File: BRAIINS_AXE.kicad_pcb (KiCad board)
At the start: 6 copper layers, 105.5 x 181.1 mm, 230 parts, among them J1 RJ45_Hanrun_HR911105A_Horizon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, J10 Connector 02x01, J2 Conn_01x06, J9 Conn_01x10, M1 Fan_4pin, M2 Fan_4pin, U10 BM1370_mode1, U11 BM1370_mode1, U15 W5500, U16 CSD95472Q5MC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

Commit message: alingment
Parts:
- moved C190 4.31 mm to (54.1, 63.5)
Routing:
- net +1V2: track 217.1 -> 216.9 mm, vias 9 -> 8
- net VDD: vias 137 -> 148
- net GND: vias 337 -> 297
- net +12V: vias 20 -> 1

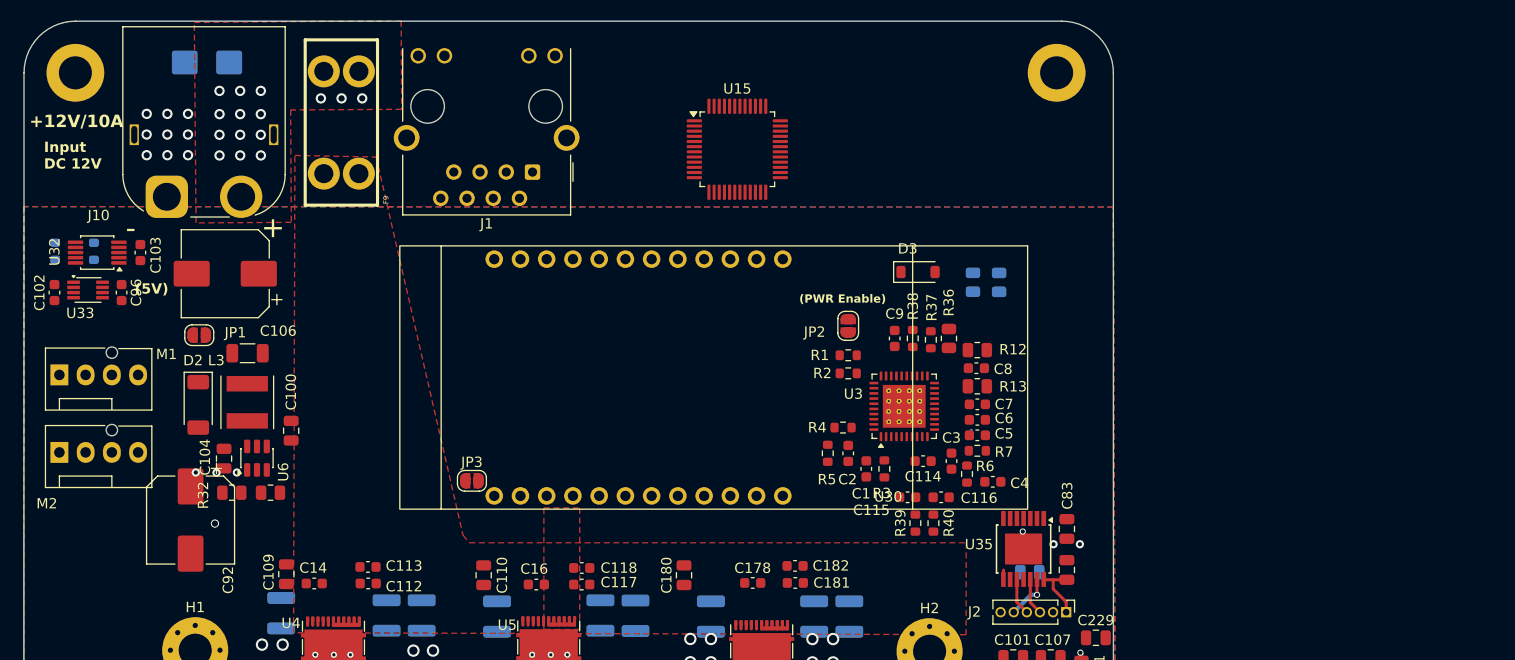
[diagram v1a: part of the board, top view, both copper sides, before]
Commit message: 3v3 eth
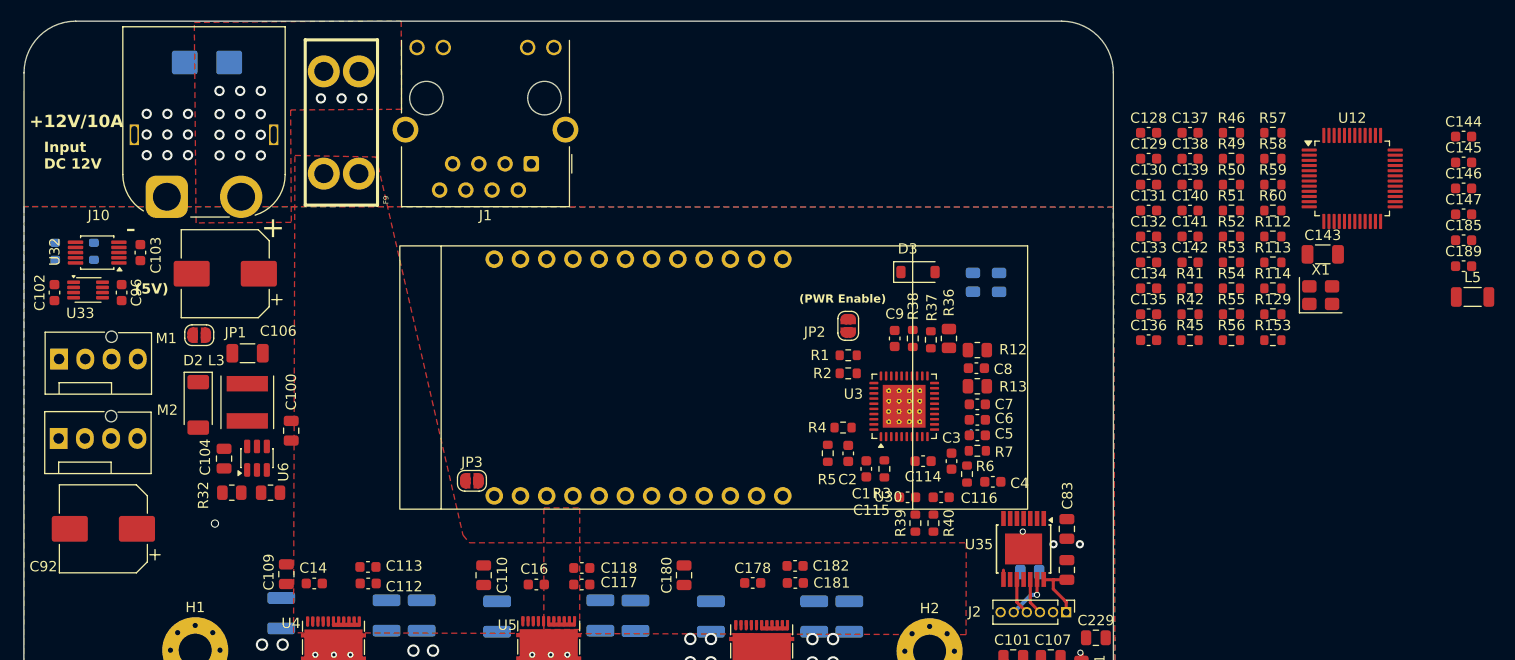
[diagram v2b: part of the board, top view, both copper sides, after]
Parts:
- removed the ? at (134.6, 44.0)
- removed the REF** at (39.6, 44.0)
- removed U15: W5500, Package_QFP:LQFP-48_7x7mm_P0.5mm
- added C128: 15pF, Capacitor_SMD:C_0603_1608Metric, F.Cu at (143.5, 49.9)
- added C129: 15pF, Capacitor_SMD:C_0603_1608Metric, F.Cu at (143.5, 52.4)
- added C130: 100nF, Capacitor_SMD:C_0603_1608Metric, F.Cu at (143.5, 54.9)
- added C131: 100nF, Capacitor_SMD:C_0603_1608Metric, F.Cu at (143.5, 57.4)
- added C132: 100nF, Capacitor_SMD:C_0603_1608Metric, F.Cu at (143.5, 59.9)
- added C133: 4.7uF, Capacitor_SMD:C_0603_1608Metric, F.Cu at (143.5, 62.4)
- added C134: 100nF, Capacitor_SMD:C_0603_1608Metric, F.Cu at (143.5, 64.9)
- added C135: 100nF, Capacitor_SMD:C_0603_1608Metric, F.Cu at (143.5, 67.4)
- added C136: 100nF, Capacitor_SMD:C_0603_1608Metric, F.Cu at (143.5, 69.9)
- added C137: 100nF, Capacitor_SMD:C_0603_1608Metric, F.Cu at (147.5, 49.9)
- added C138: 100nF, Capacitor_SMD:C_0603_1608Metric, F.Cu at (147.5, 52.4)
- added C139: 100nF, Capacitor_SMD:C_0603_1608Metric, F.Cu at (147.5, 54.9)
- added C140: 6.8nF, Capacitor_SMD:C_0603_1608Metric, F.Cu at (147.5, 57.4)
- added C141: 6.8nF, Capacitor_SMD:C_0603_1608Metric, F.Cu at (147.5, 59.9)
- added C142: 22n, Capacitor_SMD:C_0603_1608Metric, F.Cu at (147.5, 62.4)
- added C143: 1n, Capacitor_SMD:C_1206_3216Metric, F.Cu at (160.4, 61.6)
- added C144: 100nF, Capacitor_SMD:C_0603_1608Metric, F.Cu at (174.0, 50.2)
- added C145: 100nF, Capacitor_SMD:C_0603_1608Metric, F.Cu at (174.0, 52.7)
- added C146: 100nF, Capacitor_SMD:C_0603_1608Metric, F.Cu at (174.0, 55.2)
- added C147: 100nF, Capacitor_SMD:C_0603_1608Metric, F.Cu at (174.0, 57.8)
- added C185: 1u, Capacitor_SMD:C_0603_1608Metric, F.Cu at (174.0, 60.3)
- added C189: 1u, Capacitor_SMD:C_0603_1608Metric, F.Cu at (174.0, 62.8)
- added L5: MH3261-601Y, Inductor_SMD:L_1206_3216Metric, F.Cu at (174.9, 65.8)
- added R112: 0R, Resistor_SMD:R_0603_1608Metric, F.Cu at (155.5, 59.9)
- added R113: 0R, Resistor_SMD:R_0603_1608Metric, F.Cu at (155.5, 62.4)
- added R114: 0R, Resistor_SMD:R_0603_1608Metric, F.Cu at (155.5, 64.9)
- added R129: 4k7, Resistor_SMD:R_0603_1608Metric, F.Cu at (155.5, 67.4)
- added R153: 33R, Resistor_SMD:R_0603_1608Metric, F.Cu at (155.5, 69.9)
- added R41: 1M, Resistor_SMD:R_0603_1608Metric, F.Cu at (147.5, 64.9)
- added R42: 3R3, Resistor_SMD:R_0603_1608Metric, F.Cu at (147.5, 67.4)
- added R45: 3R3, Resistor_SMD:R_0603_1608Metric, F.Cu at (147.5, 69.9)
- added R46: 3R3, Resistor_SMD:R_0603_1608Metric, F.Cu at (151.5, 49.9)
- added R49: 3R3, Resistor_SMD:R_0603_1608Metric, F.Cu at (151.5, 52.4)
- added R50: 49R9, Resistor_SMD:R_0603_1608Metric, F.Cu at (151.5, 54.9)
- added R51: 12k4, Resistor_SMD:R_0603_1608Metric, F.Cu at (151.5, 57.4)
- added R52: 4k7, Resistor_SMD:R_0603_1608Metric, F.Cu at (151.5, 59.9)
- added R53: 4k7, Resistor_SMD:R_0603_1608Metric, F.Cu at (151.5, 62.4)
- added R54: 49R9, Resistor_SMD:R_0603_1608Metric, F.Cu at (151.5, 64.9)
- added R55: 49R9, Resistor_SMD:R_0603_1608Metric, F.Cu at (151.5, 67.4)
- added R56: 49R9, Resistor_SMD:R_0603_1608Metric, F.Cu at (151.5, 69.9)
- added R57: 10R, Resistor_SMD:R_0603_1608Metric, F.Cu at (155.5, 49.9)
- added R58: 330R, Resistor_SMD:R_0603_1608Metric, F.Cu at (155.5, 52.4)
- added R59: 330R, Resistor_SMD:R_0603_1608Metric, F.Cu at (155.5, 54.9)
- added R60: 1M, Resistor_SMD:R_0603_1608Metric, F.Cu at (155.5, 57.4)
- added U12: W5500, Package_QFP:LQFP-48_7x7mm_P0.5mm, F.Cu at (163.2, 54.3)
- added X1: TXM25M0004322JBDDO00T, Crystal:Crystal_SMD_3225-4Pin_3.2x2.5mm, F.Cu at (160.2, 65.6)
- moved C92 8.49 mm to (42.3, 88.2), turned to 180 degrees
- moved M1 1.54 mm to (38.0, 71.8)
- moved M2 1.35 mm to (38.0, 79.5)
- moved J1 0.81 mm to (83.7, 52.9)
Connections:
- J1 pad 1: unconnected-(J1-TD+-Pad1) -> /controller/ETH_TX_P
- J1 pad 10: unconnected-(J1-Pad10) -> /controller/ACT_LED_N
- J1 pad 11: unconnected-(J1-Pad11) -> /controller/LINK_LED_N
- J1 pad 12: unconnected-(J1-Pad12) -> Net-(J1-Pad12)
- J1 pad 2: unconnected-(J1-TD--Pad2) -> /controller/ETH_TX_N
- J1 pad 3: unconnected-(J1-RD+-Pad3) -> /controller/ETH_RX_P
- J1 pad 4: unconnected-(J1-TCT-Pad4) -> Net-(J1-TCT)
- J1 pad 5: unconnected-(J1-RCT-Pad5) -> Net-(J1-RCT)
- J1 pad 6: unconnected-(J1-RD--Pad6) -> /controller/ETH_RX_N
- J1 pad 8: unconnected-(J1-Pad8) -> FGND
- J1 pad 9: unconnected-(J1-Pad9) -> Net-(J1-Pad9)
- J1 pad SH: unconnected-(J1-PadSH) -> FGND
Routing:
- net GND: vias 297 -> 294
